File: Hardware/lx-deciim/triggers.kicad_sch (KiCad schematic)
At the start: 86 parts, among them J1 AudioJack2_SwitchT, J10 AudioJack2_SwitchT, J11 AudioJack2_SwitchT, J12 AudioJack2_SwitchT, J18 Conn_01x15_Pin, J19 Conn_01x15_Socket, J2 AudioJack2_SwitchT, J20 Conn_01x15_Pin, J21 Conn_01x15_Socket, J3 AudioJack2_SwitchT, J4 AudioJack2_SwitchT, J5 AudioJack2_SwitchT, J6 AudioJack2_SwitchT, J7 AudioJack2_SwitchT, J8 AudioJack2_SwitchT, J9 AudioJack2_SwitchT, U1 MCP6004, U2 MCP6001-OT, U3 MCP6004, U4 MCP6004

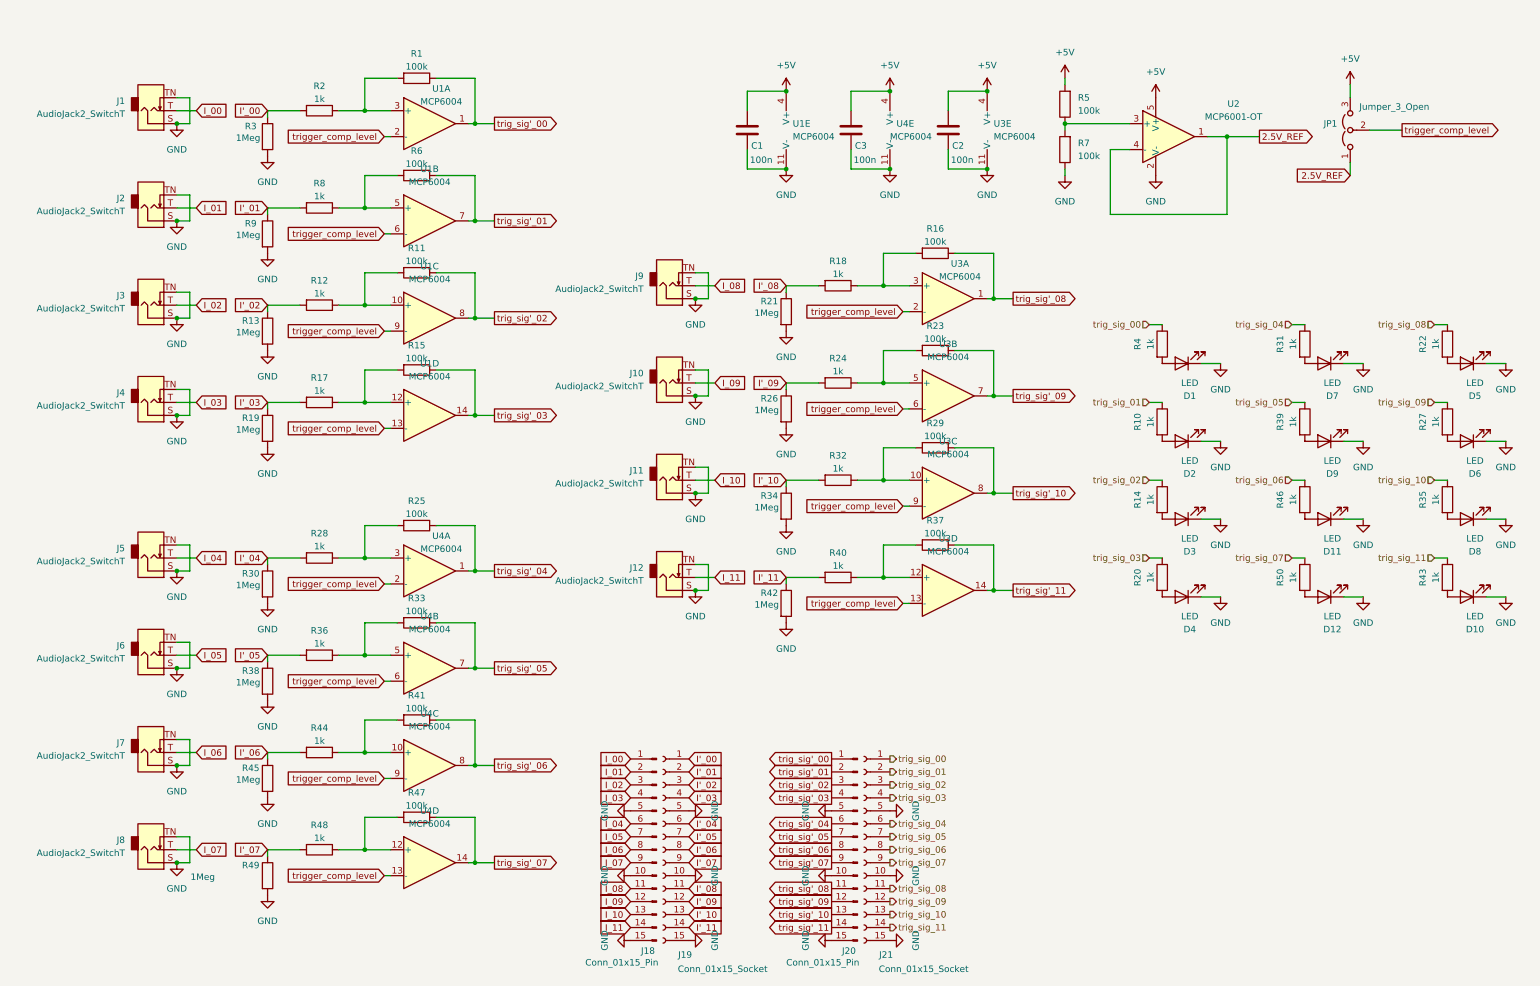
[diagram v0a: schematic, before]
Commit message: feature: first draft routing
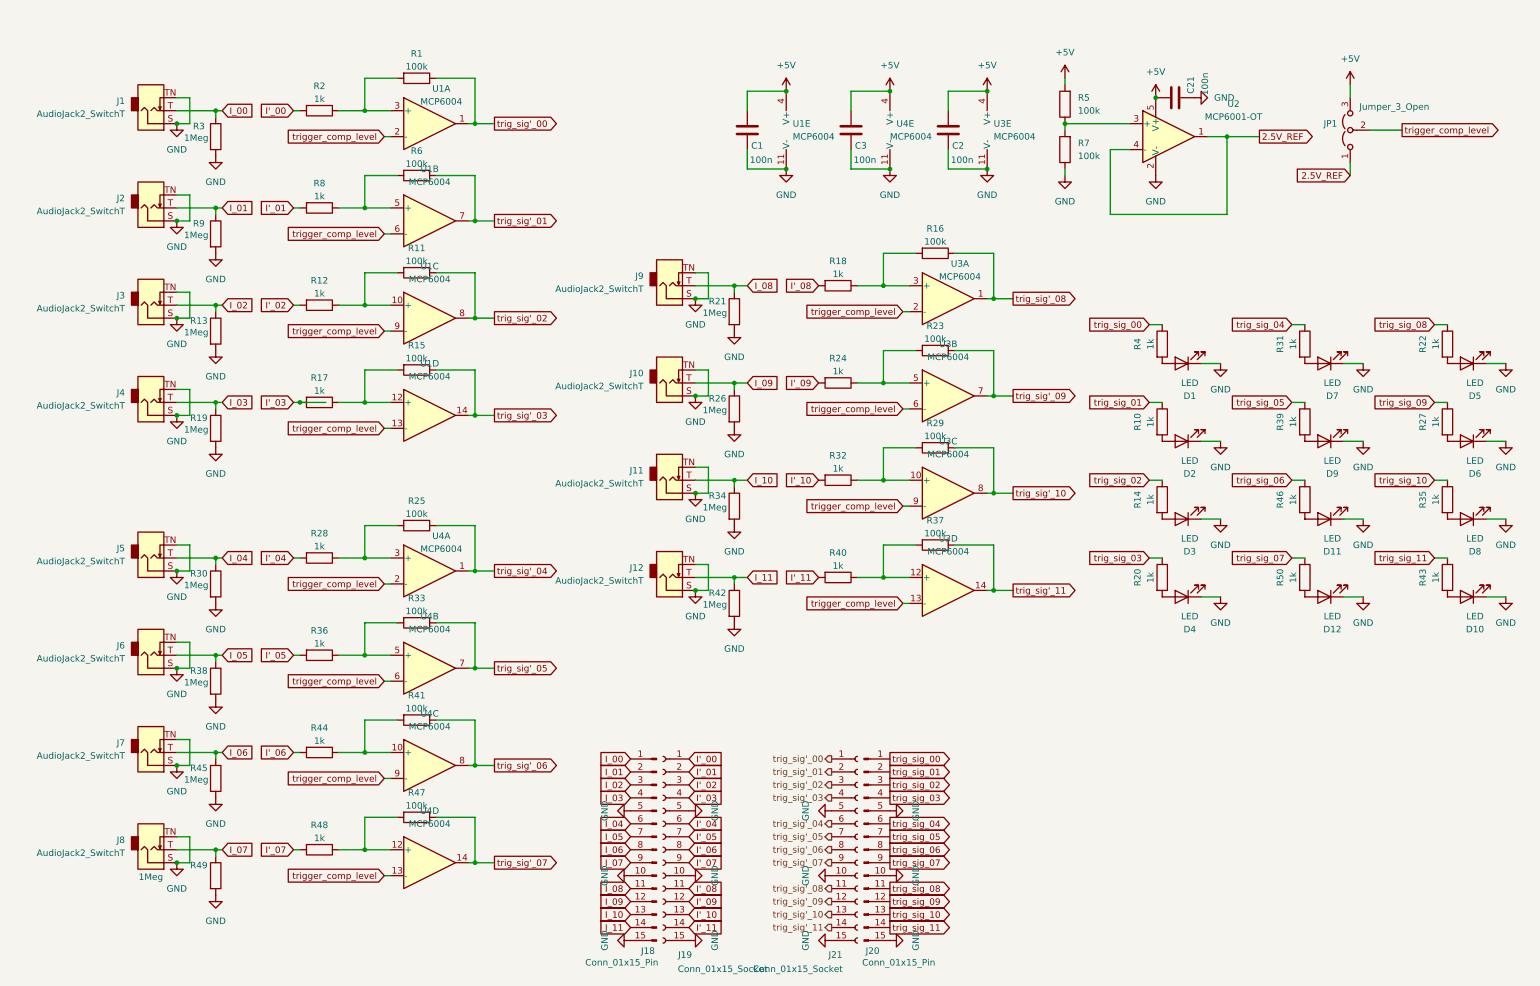
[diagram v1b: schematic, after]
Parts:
- added C21: 100n, Capacitor_SMD:C_0603_1608Metric, symbol Device:C
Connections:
- net +5V: now also C21.1
- net GND: now also C21.2
- net I'_00: no longer R3.1
- net I'_01: no longer R9.1
- net I'_02: no longer R13.1
- net I'_03: no longer R19.1
- net I'_04: no longer R30.1
- net I'_05: no longer R38.1
- net I'_06: no longer R45.1
- net I'_07: no longer R49.1
- net I'_08: no longer R21.1
- net I'_09: no longer R26.1
- net I'_10: no longer R34.1
- net I'_11: no longer R42.1
- net I_00: now also R3.1
- net I_01: now also R9.1
- net I_02: now also R13.1
- net I_03: now also R19.1
- net I_04: now also R30.1
- net I_05: now also R38.1
- net I_06: now also R45.1
- net I_07: now also R49.1
- net I_08: now also R21.1
- net I_09: now also R26.1
- net I_10: now also R34.1
- net I_11: now also R42.1
- net trig_sig'_00: now also J21.1 (Pin_1); no longer J20.1 (Pin_1)
- net trig_sig'_01: now also J21.2 (Pin_2); no longer J20.2 (Pin_2)
- net trig_sig'_02: now also J21.3 (Pin_3); no longer J20.3 (Pin_3)
- net trig_sig'_03: now also J21.4 (Pin_4); no longer J20.4 (Pin_4)
- net trig_sig'_04: now also J21.6 (Pin_6); no longer J20.6 (Pin_6)
- net trig_sig'_05: now also J21.7 (Pin_7); no longer J20.7 (Pin_7)
- net trig_sig'_06: now also J21.8 (Pin_8); no longer J20.8 (Pin_8)
- net trig_sig'_07: now also J21.9 (Pin_9); no longer J20.9 (Pin_9)
- net trig_sig'_08: now also J21.11 (Pin_11); no longer J20.11 (Pin_11)
- net trig_sig'_09: now also J21.12 (Pin_12); no longer J20.12 (Pin_12)
- net trig_sig'_10: now also J21.13 (Pin_13); no longer J20.13 (Pin_13)
- net trig_sig'_11: now also J21.14 (Pin_14); no longer J20.14 (Pin_14)
- net trig_sig_00: now also J20.1 (Pin_1); no longer J21.1 (Pin_1)
- net trig_sig_01: now also J20.2 (Pin_2); no longer J21.2 (Pin_2)
- net trig_sig_02: now also J20.3 (Pin_3); no longer J21.3 (Pin_3)
- net trig_sig_03: now also J20.4 (Pin_4); no longer J21.4 (Pin_4)
- net trig_sig_04: now also J20.6 (Pin_6); no longer J21.6 (Pin_6)
- net trig_sig_05: now also J20.7 (Pin_7); no longer J21.7 (Pin_7)
- net trig_sig_06: now also J20.8 (Pin_8); no longer J21.8 (Pin_8)
- net trig_sig_07: now also J20.9 (Pin_9); no longer J21.9 (Pin_9)
- net trig_sig_08: now also J20.11 (Pin_11); no longer J21.11 (Pin_11)
- net trig_sig_09: now also J20.12 (Pin_12); no longer J21.12 (Pin_12)
- net trig_sig_10: now also J20.13 (Pin_13); no longer J21.13 (Pin_13)
- net trig_sig_11: now also J20.14 (Pin_14); no longer J21.14 (Pin_14)
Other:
- moved on the sheet: J20, J21, R13, R19, R21, R26, R3, R30, R34, R38, R42, R45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

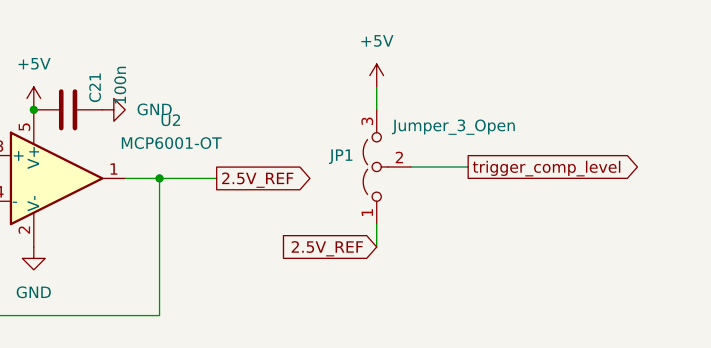
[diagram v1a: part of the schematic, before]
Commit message: feature: clean routing
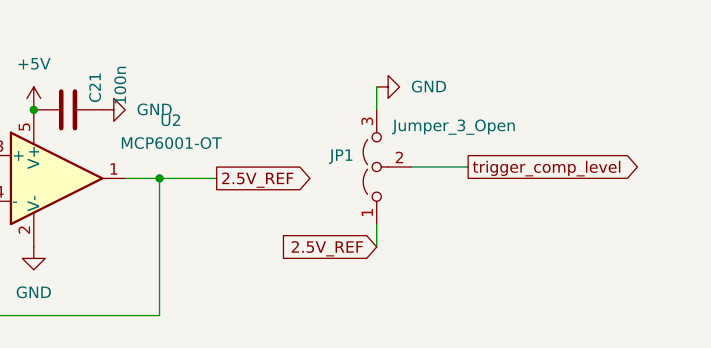
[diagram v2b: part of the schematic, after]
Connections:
- net +5V: no longer JP1.3 (B)
- net GND: now also JP1.3 (B)
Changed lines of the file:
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@@
-	)
-	(symbol
-		(lib_id "power:+5V")
-		(at 252.73 20.32 0)
-		(unit 1)
-		(exclude_from_sim no)
-		(in_bom yes)
-		(on_board yes)
-		(dnp no)
-		(fields_autoplaced yes)
-		(property "Reference" "#PWR010"
-			(at 252.73 24.13 0)
-			(effects
-				(font
-					(size 1.27 1.27)
-				)
-				(hide yes)
-			)
-		)
-		(property "Value" "+5V"
-			(at 252.73 15.24 0)
-			(effects
-				(font
-					(size 1.27 1.27)
-				)
-			)
-		)
-		(property "Footprint" ""
-			(at 252.73 20.32 0)
-			(effects
-				(font
-					(size 1.27 1.27)
-				)
-				(hide yes)
-			)
-		)
-		(property "Datasheet" ""
-			(at 252.73 20.32 0)
-			(effects
-				(font
-					(size 1.27 1.27)
-				)
-				(hide yes)
-			)
-		)
-		(property "Description" "Power symbol creates a global label with name \"+5V\""
-			(at 252.73 20.32 0)
-			(effects
-				(font
-					(size 1.27 1.27)
-				)
-				(hide yes)
-			)
-		)
-		(pin "1"
-		)
-		(instances
-			(project "lx-deciim"
-				(path "/9ca2396d-dee1-4fae-99da-0a85948cf9d5/ab19b4a5-9c44-4120-a39c-ac50899822bb"
-					(reference "#PWR010")
-					(unit 1)
-				)
-			)
-		)
 	)
 	(symbol
@@
 				)
 			)
+		)
+	)
+	(symbol
+		(lib_id "power:GND")
+		(at 252.73 20.32 90)
+		(unit 1)
+		(exclude_from_sim no)
+		(in_bom yes)
+		(on_board yes)
+		(dnp no)
+		(fields_autoplaced yes)
+		(property "Reference" "#PWR0109"
+			(at 259.08 20.32 0)
+			(effects
+				(font
+					(size 1.27 1.27)
+				)
+				(hide yes)
+			)
+		)
+		(property "Value" "GND"
+			(at 256.54 20.3199 90)
+			(effects
+				(font
+					(size 1.27 1.27)
+				)
+				(justify right)
+			)
+		)
+		(property "Footprint" ""
+			(at 252.73 20.32 0)
+			(effects
+				(font
+					(size 1.27 1.27)
+				)
+				(hide yes)
+			)
+		)
+		(property "Datasheet" ""
+			(at 252.73 20.32 0)
+			(effects
+				(font
+					(size 1.27 1.27)
+				)
+				(hide yes)
+			)
+		)
+		(property "Description" "Power symbol creates a global label with name \"GND\" , ground"
+			(at 252.73 20.32 0)
+			(effects
+				(font
+					(size 1.27 1.27)
+				)
+				(hide yes)
+			)
+		)
+		(pin "1"
+		)
+		(instances
+			(project "lx-deciim"
+				(path "/9ca2396d-dee1-4fae-99da-0a85948cf9d5/ab19b4a5-9c44-4120-a39c-ac50899822bb"
+					(reference "#PWR0109")
+					(unit 1)
+				)
+			)

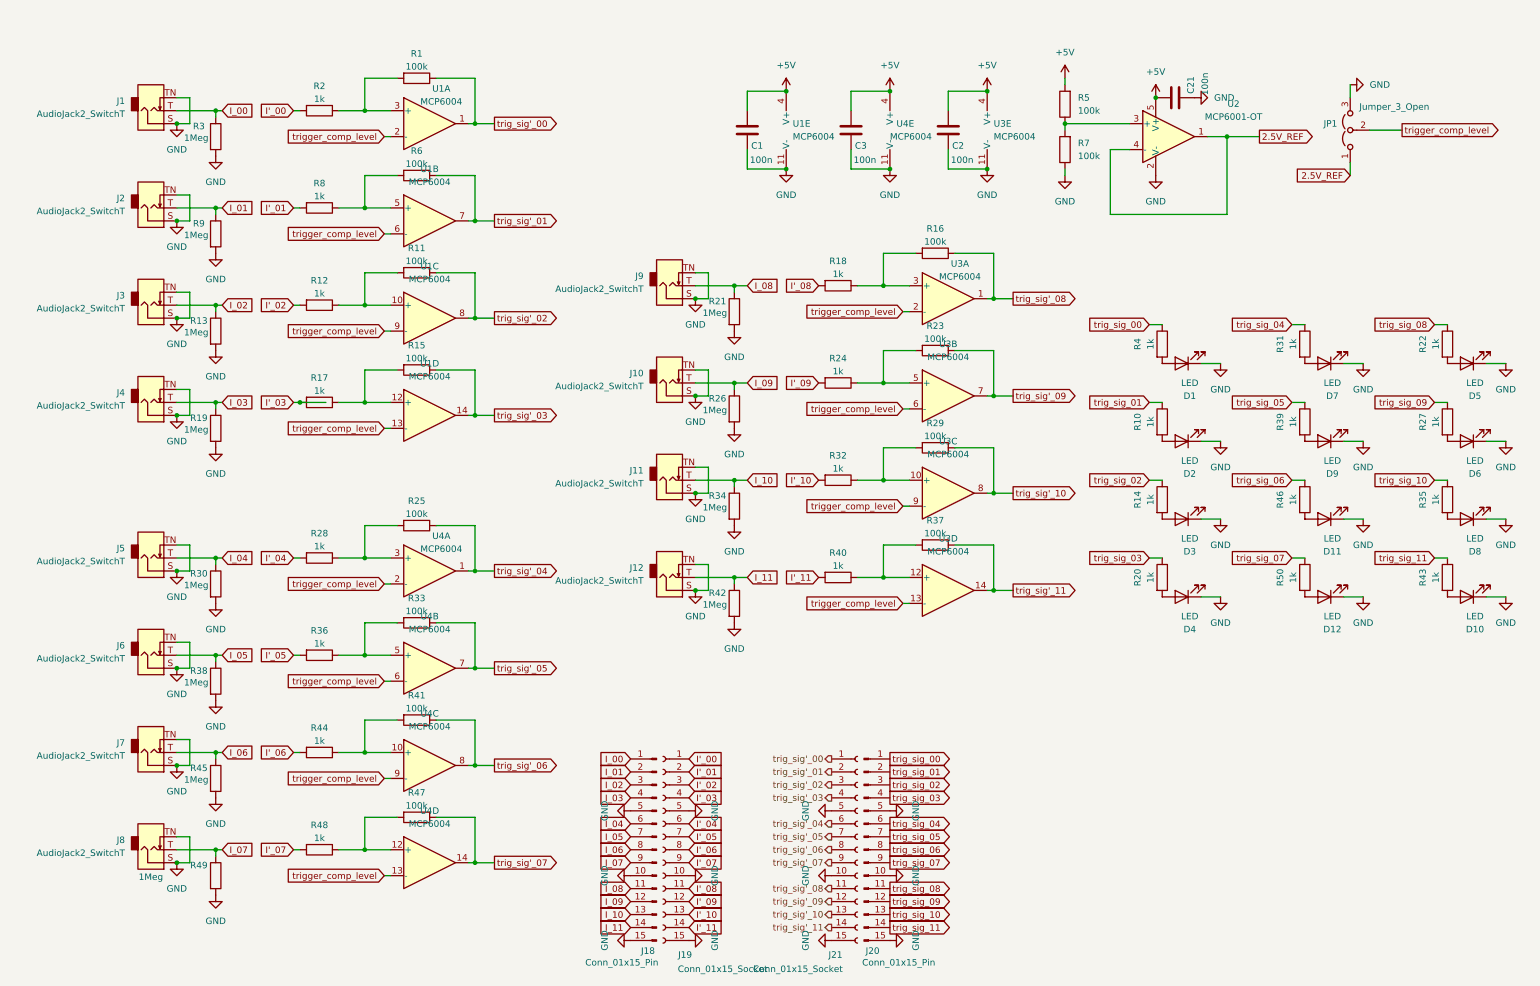
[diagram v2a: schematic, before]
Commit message: feature: prep files for export (fill bom, gerber)
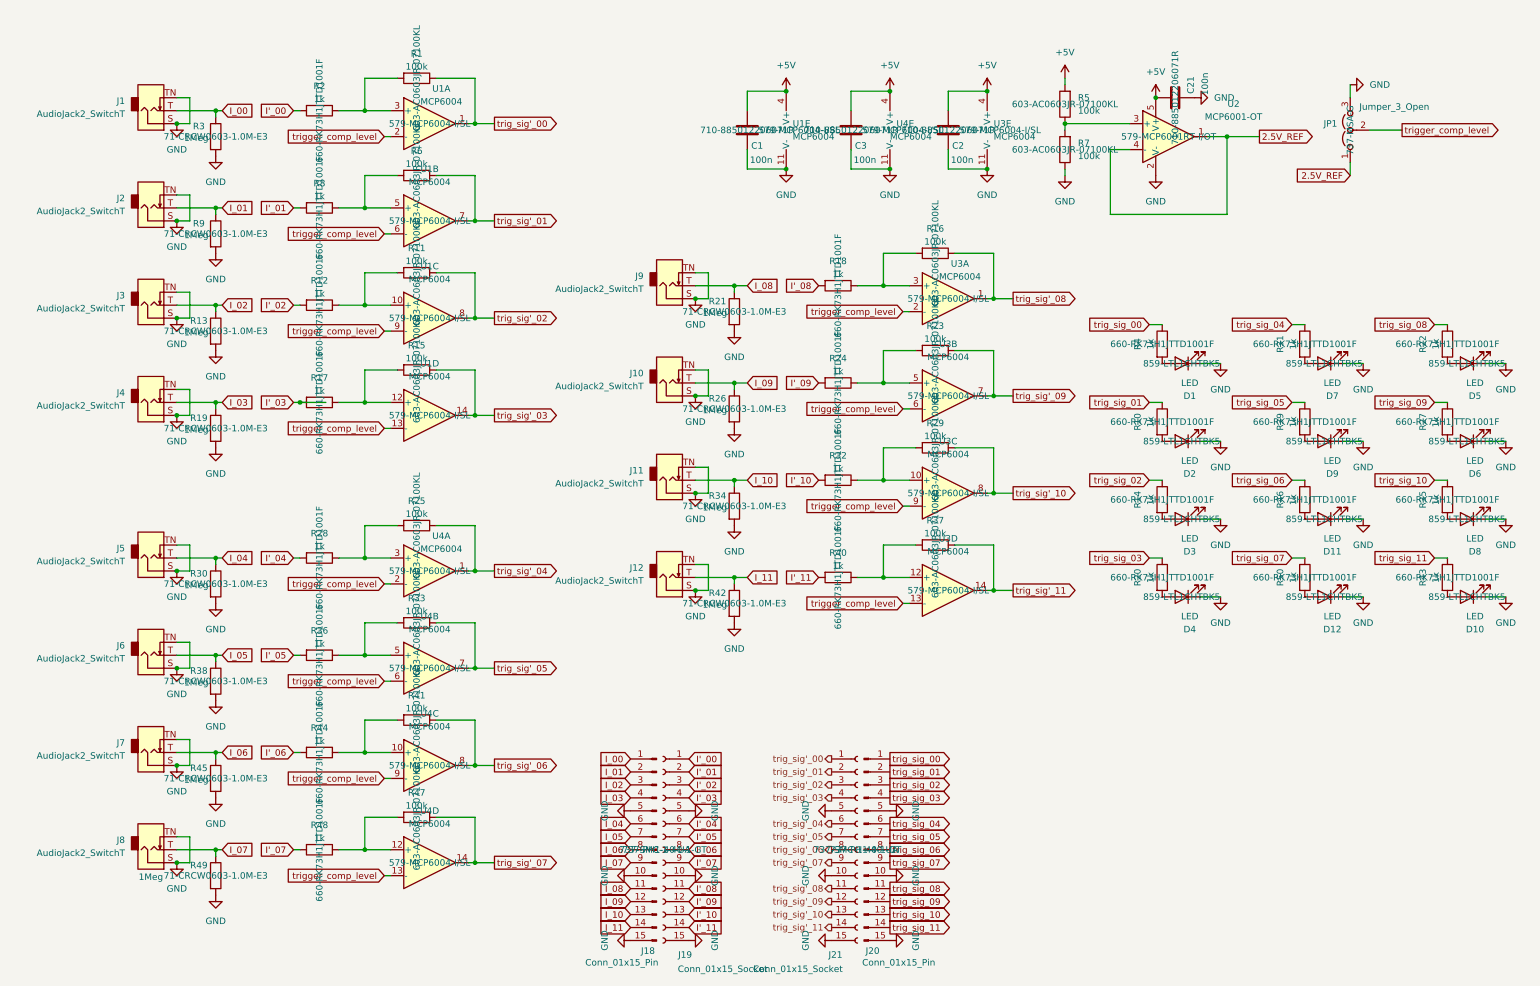
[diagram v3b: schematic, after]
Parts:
- C1, C2, C21, C3: Mouser Part Number (none) -> 710-885012206071R
- D1, D10, D11, D12, D2, D3, D4, D5, D6, D7, D8, D9: Mouser Part Number (none) -> 859-LTL1CHTBK5
- J18, J20: Mouser Part Number (none) -> 737-PH1-40-UA
- J19, J21: Mouser Part Number (none) -> 737-SMC-1-40-1-GT
- JP1: Mouser Part Number (none) -> 737-MSA-G
- R1, R11, R15, R16, R23, R25, R29, R33, R37, R41, R47, R5, R6, R7: Mouser Part Number (none) -> 603-AC0603JR-07100KL
- R10, R12, R14, R17, R18, R2, R20, R22, R24, R27, R28, R31, R32, R35, R36, R39, R4, R40, R43, R44, R46, R48, R50, R8: Mouser Part Number (none) -> 660-RK73H1JTTD1001F
- R13, R19, R21, R26, R3, R30, R34, R38, R42, R45, R49, R9: Mouser Part Number (none) -> 71-CRCW0603-1.0M-E3
- U1, U3, U4: Mouser Part Number (none) -> 579-MCP6004-I/SL
- U2: Mouser Part Number (none) -> 579-MCP6001RT-I/OT

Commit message: fix: fix mouser part number on schematic + fill page settings
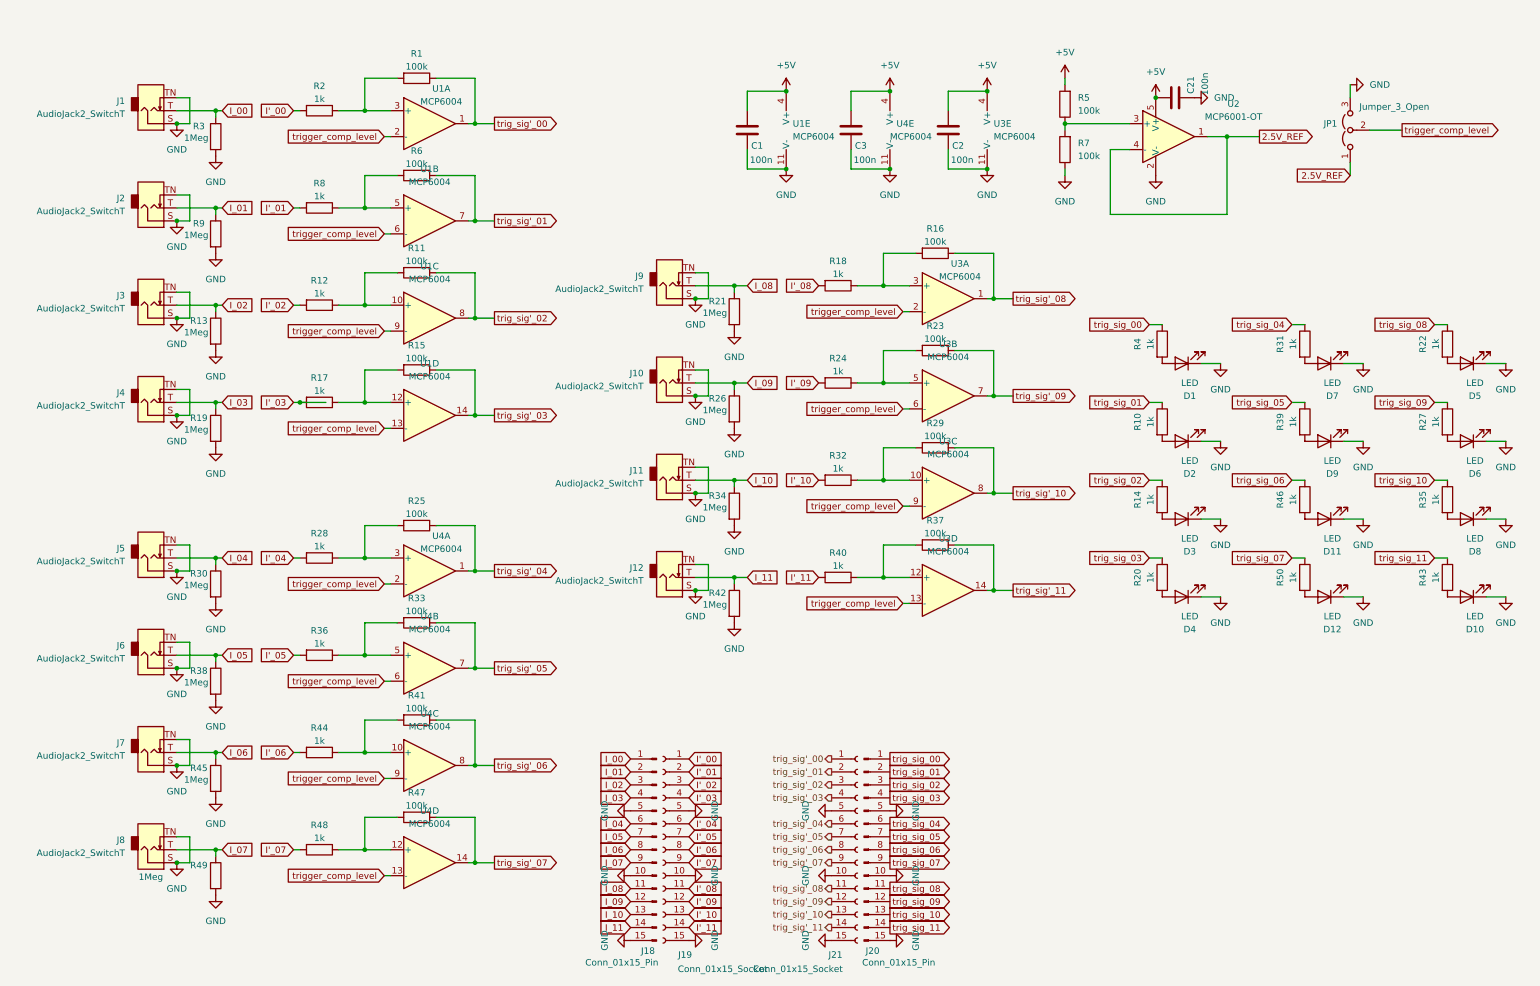
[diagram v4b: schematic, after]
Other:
- company: (none) -> Lucas Bonvin
- title: (none) -> lx-deciim
